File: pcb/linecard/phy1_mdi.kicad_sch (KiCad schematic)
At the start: 51 parts, among them J5 LPJT476156AENL, J9 LPJT476156AENL, U35 VSC8512, U36 ESD224DQAR, U37 ESD224DQAR, U38 ESD224DQAR, U39 ESD224DQAR, U40 ESD224DQAR, U41 ESD224DQAR, U42 ESD224DQAR, U43 ESD224DQAR, U44 ESD224DQAR, U45 ESD224DQAR, U46 ESD224DQAR, U47 ESD224DQAR, U48 ESD224DQAR, U49 ESD224DQAR, U50 ESD224DQAR, U51 ESD224DQAR, U52 ESD224DQAR, U53 ESD224DQAR, U54 ESD224DQAR, U55 ESD224DQAR, U56 ESD224DQAR, U57 ESD224DQAR, U58 ESD224DQAR, U59 ESD224DQAR

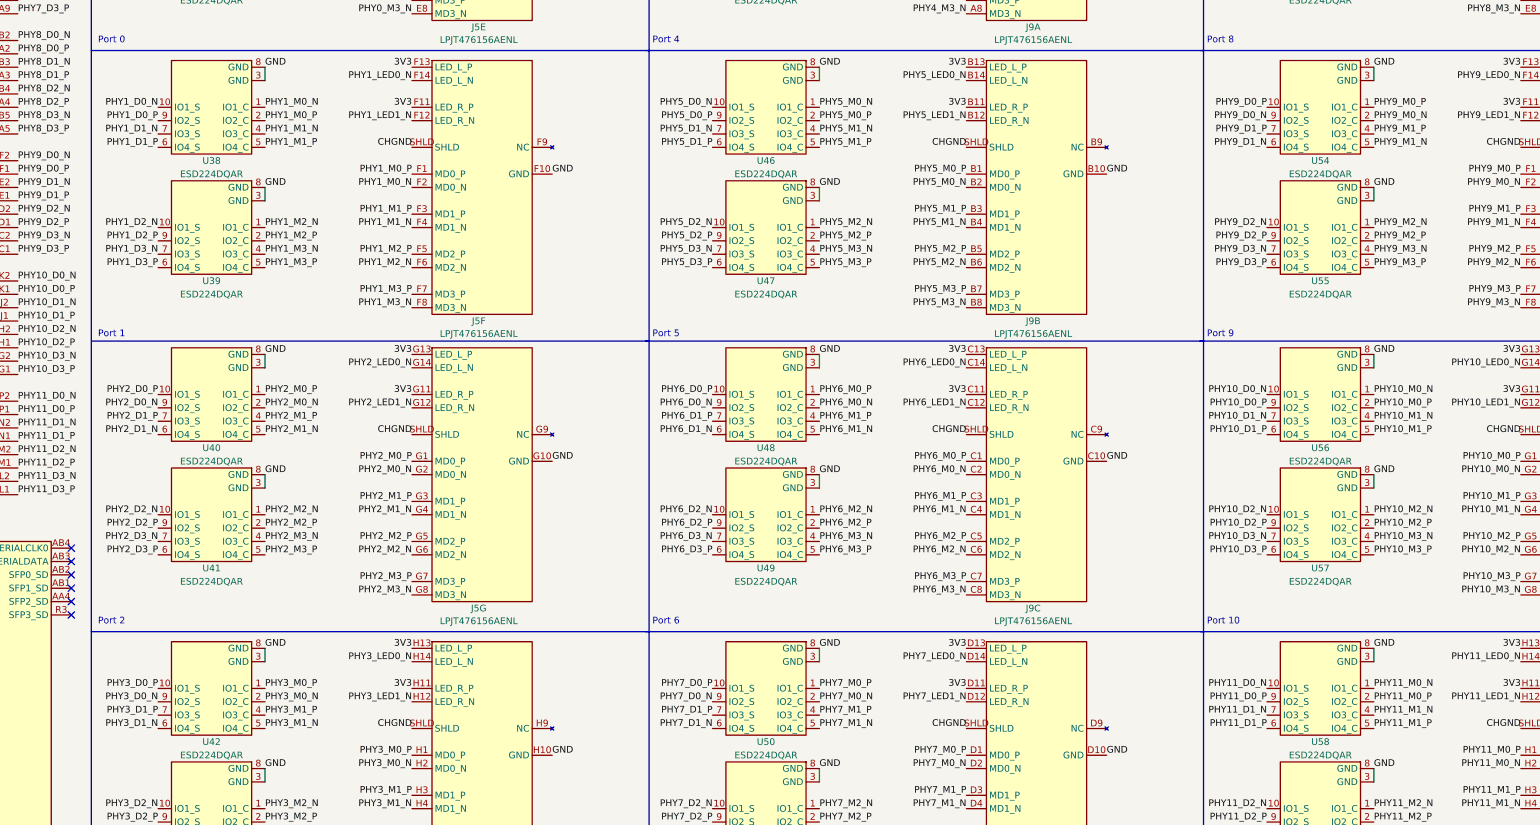
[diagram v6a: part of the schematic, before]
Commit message: Continued tying up loose ends on routing of left side and supervisor
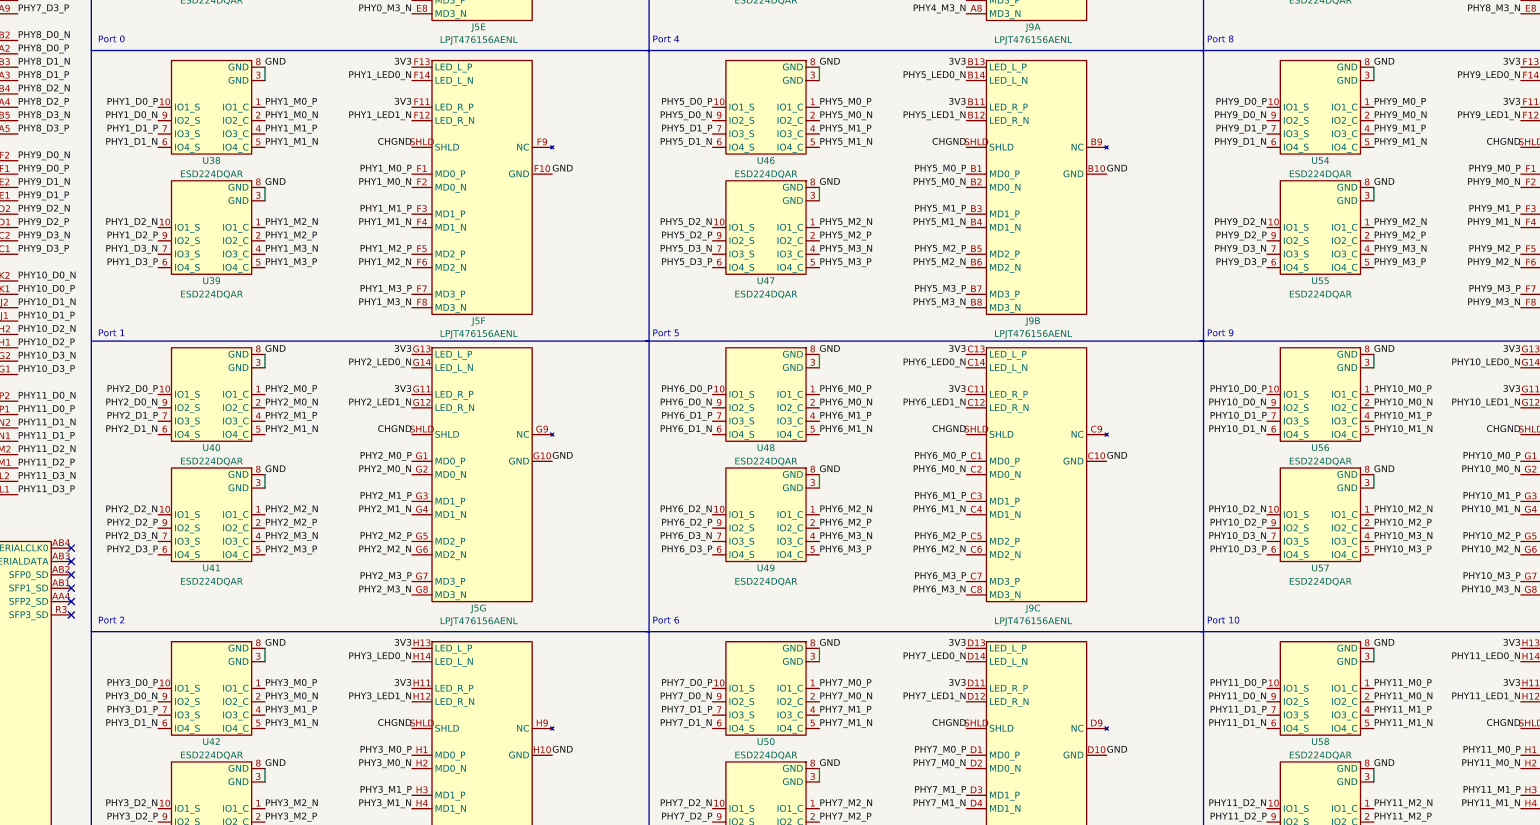
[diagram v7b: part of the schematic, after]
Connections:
- net PHY10_D0_N: now also U56.9 (IO2_S); no longer U56.10 (IO1_S)
- net PHY10_D0_P: now also U56.10 (IO1_S); no longer U56.9 (IO2_S)
- net PHY10_D1_N: now also U56.6 (IO4_S); no longer U56.7 (IO3_S)
- net PHY10_D1_P: now also U56.7 (IO3_S); no longer U56.6 (IO4_S)
- net PHY10_M0_N: now also U56.2 (IO2_C); no longer U56.1 (IO1_C)
- net PHY10_M0_P: now also U56.1 (IO1_C); no longer U56.2 (IO2_C)
- net PHY10_M1_N: now also U56.5 (IO4_C); no longer U56.4 (IO3_C)
- net PHY10_M1_P: now also U56.4 (IO3_C); no longer U56.5 (IO4_C)
- net PHY11_D0_N: now also U58.9 (IO2_S); no longer U58.10 (IO1_S)
- net PHY11_D0_P: now also U58.10 (IO1_S); no longer U58.9 (IO2_S)
- net PHY11_D1_N: now also U58.6 (IO4_S); no longer U58.7 (IO3_S)
- net PHY11_D1_P: now also U58.7 (IO3_S); no longer U58.6 (IO4_S)
- net PHY11_M0_N: now also U58.2 (IO2_C); no longer U58.1 (IO1_C)
- net PHY11_M0_P: now also U58.1 (IO1_C); no longer U58.2 (IO2_C)
- net PHY11_M1_N: now also U58.5 (IO4_C); no longer U58.4 (IO3_C)
- net PHY11_M1_P: now also U58.4 (IO3_C); no longer U58.5 (IO4_C)
- net PHY1_D0_N: now also U38.9 (IO2_S); no longer U38.10 (IO1_S)
- net PHY1_D0_P: now also U38.10 (IO1_S); no longer U38.9 (IO2_S)
- net PHY1_D1_N: now also U38.6 (IO4_S); no longer U38.7 (IO3_S)
- net PHY1_D1_P: now also U38.7 (IO3_S); no longer U38.6 (IO4_S)
- net PHY1_M0_N: now also U38.2 (IO2_C); no longer U38.1 (IO1_C)
- net PHY1_M0_P: now also U38.1 (IO1_C); no longer U38.2 (IO2_C)
- net PHY1_M1_N: now also U38.5 (IO4_C); no longer U38.4 (IO3_C)
- net PHY1_M1_P: now also U38.4 (IO3_C); no longer U38.5 (IO4_C)
- net PHY5_D0_N: now also U46.9 (IO2_S); no longer U46.10 (IO1_S)
- net PHY5_D0_P: now also U46.10 (IO1_S); no longer U46.9 (IO2_S)
- net PHY5_D1_N: now also U46.6 (IO4_S); no longer U46.7 (IO3_S)
- net PHY5_D1_P: now also U46.7 (IO3_S); no longer U46.6 (IO4_S)
- net PHY5_M0_N: now also U46.2 (IO2_C); no longer U46.1 (IO1_C)
- net PHY5_M0_P: now also U46.1 (IO1_C); no longer U46.2 (IO2_C)
- net PHY5_M1_N: now also U46.5 (IO4_C); no longer U46.4 (IO3_C)
- net PHY5_M1_P: now also U46.4 (IO3_C); no longer U46.5 (IO4_C)
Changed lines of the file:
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@@
 	(title_block
 		(title "LATENTRED Line Card")
-		(date "2024-12-17")
+		(date "2024-12-18")
 		(rev "0.1")
 		(company "Antikernel Labs")
@@
 	)
 	(label "PHY11_M1_P"
-		(at 334.01 196.85 0)
+		(at 334.01 194.31 0)
 		(fields_autoplaced yes)
 		(effects
@@
 	)
 	(label "PHY1_D1_N"
-		(at 102.87 83.82 180)
+		(at 102.87 86.36 180)
 		(fields_autoplaced yes)
 		(effects
@@
 	)
 	(label "PHY1_M0_N"
-		(at 123.19 78.74 0)
+		(at 123.19 81.28 0)
 		(fields_autoplaced yes)
 		(effects
@@
 	)
 	(label "PHY5_M0_N"
-		(at 228.6 78.74 0)
+		(at 228.6 81.28 0)
 		(fields_autoplaced yes)
 		(effects
@@
 	)
 	(label "PHY5_D1_N"
-		(at 208.28 83.82 180)
+		(at 208.28 86.36 180)
 		(fields_autoplaced yes)
 		(effects
@@
 	)
 	(label "PHY11_M0_N"
-		(at 334.01 189.23 0)
+		(at 334.01 191.77 0)
 		(fields_autoplaced yes)
 		(effects
@@
 	)
 	(label "PHY5_D0_P"
-		(at 208.28 81.28 180)
+		(at 208.28 78.74 180)
 		(fields_autoplaced yes)
 		(effects
@@
 	)
 	(label "PHY10_M0_P"
-		(at 334.01 135.89 0)
+		(at 334.01 133.35 0)
 		(fields_autoplaced yes)
 		(effects
@@
 	)
 	(label "PHY5_D1_P"
-		(at 208.28 86.36 180)
+		(at 208.28 83.82 180)
 		(fields_autoplaced yes)
 		(effects
@@
 	)
 	(label "PHY11_D1_P"
-		(at 313.69 196.85 180)
+		(at 313.69 194.31 180)
 		(fields_autoplaced yes)
 		(effects
@@
 	)
 	(label "PHY11_M1_N"
-		(at 334.01 194.31 0)
+		(at 334.01 196.85 0)
 		(fields_autoplaced yes)
 		(effects
@@
 	)
 	(label "PHY10_D1_P"
-		(at 313.69 140.97 180)
+		(at 313.69 138.43 180)
 		(fields_autoplaced yes)
 		(effects
@@
 	)
 	(label "PHY1_M1_N"
-		(at 123.19 83.82 0)
+		(at 123.19 86.36 0)
 		(fields_autoplaced yes)
 		(effects
@@
 	)
 	(label "PHY11_D1_N"
-		(at 313.69 194.31 180)
+		(at 313.69 196.85 180)
 		(fields_autoplaced yes)
 		(effects
@@
 	)
 	(label "PHY10_M0_N"
-		(at 334.01 133.35 0)
+		(at 334.01 135.89 0)
 		(fields_autoplaced yes)
 		(effects
@@
 	)
 	(label "PHY11_D0_P"
-		(at 313.69 191.77 180)
+		(at 313.69 189.23 180)
 		(fields_autoplaced yes)
 		(effects
@@
 	)
 	(label "PHY11_D0_N"
-		(at 313.69 189.23 180)
+		(at 313.69 191.77 180)
 		(fields_autoplaced yes)
 		(effects
@@
 	)
 	(label "PHY1_M0_P"
-		(at 123.19 81.28 0)
+		(at 123.19 78.74 0)
 		(fields_autoplaced yes)
 		(effects
@@
 	)
 	(label "PHY5_D0_N"
-		(at 208.28 78.74 180)
+		(at 208.28 81.28 180)
 		(fields_autoplaced yes)
 		(effects
@@
 	)
 	(label "PHY10_D1_N"
-		(at 313.69 138.43 180)
+		(at 313.69 140.97 180)
 		(fields_autoplaced yes)
 		(effects
@@
 	)
 	(label "PHY1_D0_N"
-		(at 102.87 78.74 180)
+		(at 102.87 81.28 180)
 		(fields_autoplaced yes)
 		(effects
@@
 	)
 	(label "PHY1_D1_P"
-		(at 102.87 86.36 180)
+		(at 102.87 83.82 180)
 		(fields_autoplaced yes)
 		(effects
@@
 	)
 	(label "PHY5_M1_N"
-		(at 228.6 83.82 0)
+		(at 228.6 86.36 0)
 		(fields_autoplaced yes)
 		(effects
@@
 	)
 	(label "PHY5_M1_P"
-		(at 228.6 86.36 0)
+		(at 228.6 83.82 0)
 		(fields_autoplaced yes)
 		(effects
@@
 	)
 	(label "PHY10_M1_P"
-		(at 334.01 140.97 0)
+		(at 334.01 138.43 0)
 		(fields_autoplaced yes)
 		(effects
@@
 	)
 	(label "PHY5_M0_P"
-		(at 228.6 81.28 0)
+		(at 228.6 78.74 0)
 		(fields_autoplaced yes)
 		(effects
@@
 	)
 	(label "PHY10_M1_N"
-		(at 334.01 138.43 0)
+		(at 334.01 140.97 0)
 		(fields_autoplaced yes)
 		(effects
@@
 	)
 	(label "PHY10_D0_P"
-		(at 313.69 135.89 180)
+		(at 313.69 133.35 180)
 		(fields_autoplaced yes)
 		(effects
@@
 	)
 	(label "PHY1_D0_P"
-		(at 102.87 81.28 180)
+		(at 102.87 78.74 180)
 		(fields_autoplaced yes)
 		(effects
@@
 	)
 	(label "PHY1_M1_P"
-		(at 123.19 86.36 0)
+		(at 123.19 83.82 0)
 		(fields_autoplaced yes)
 		(effects
@@
 	)
 	(label "PHY10_D0_N"
-		(at 313.69 133.35 180)
+		(at 313.69 135.89 180)
 		(fields_autoplaced yes)
 		(effects
@@
 	)
 	(label "PHY11_M0_P"
-		(at 334.01 191.77 0)
+		(at 334.01 189.23 0)
 		(fields_autoplaced yes)
 		(effects
